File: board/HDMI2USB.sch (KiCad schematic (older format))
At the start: 0 parts

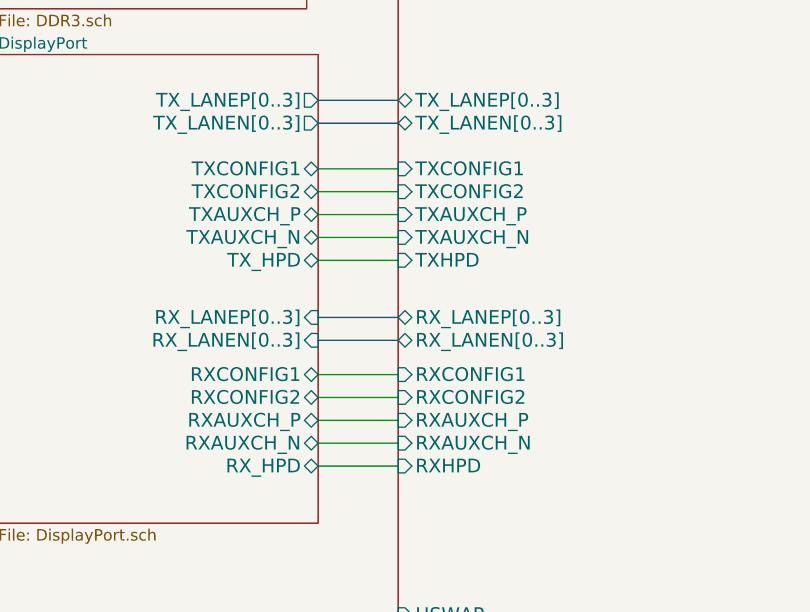
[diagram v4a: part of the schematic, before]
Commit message: Issue #1471 - usb Sheet changes
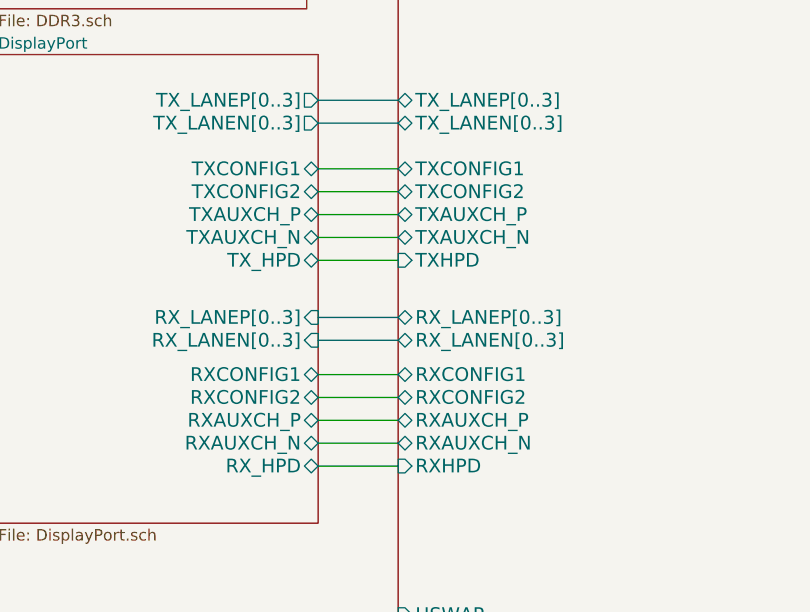
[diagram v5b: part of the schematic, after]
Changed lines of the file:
@@
 F22 "TX_LANEN[0..3]" B L 3750 4400 60
 F23 "TX_LANEP[0..3]" B L 3750 4300 60
-F24 "TXCONFIG1" I L 3750 4600 60
-F25 "TXCONFIG2" I L 3750 4700 60
-F26 "TXAUXCH_P" I L 3750 4800 60
-F27 "TXAUXCH_N" I L 3750 4900 60
+F24 "TXCONFIG1" B L 3750 4600 60
+F25 "TXCONFIG2" B L 3750 4700 60
+F26 "TXAUXCH_P" B L 3750 4800 60
+F27 "TXAUXCH_N" B L 3750 4900 60
 F28 "TXHPD" I L 3750 5000 60
-F29 "RXCONFIG1" I L 3750 5500 60
-F30 "RXCONFIG2" I L 3750 5600 60
-F31 "RXAUXCH_P" I L 3750 5700 60
+F29 "RXCONFIG1" B L 3750 5500 60
+F30 "RXCONFIG2" B L 3750 5600 60
+F31 "RXAUXCH_P" B L 3750 5700 60
 F32 "RXHPD" I L 3750 5900 60
-F33 "RXAUXCH_N" I L 3750 5800 60
+F33 "RXAUXCH_N" B L 3750 5800 60
 $EndSheet
 $Sheet

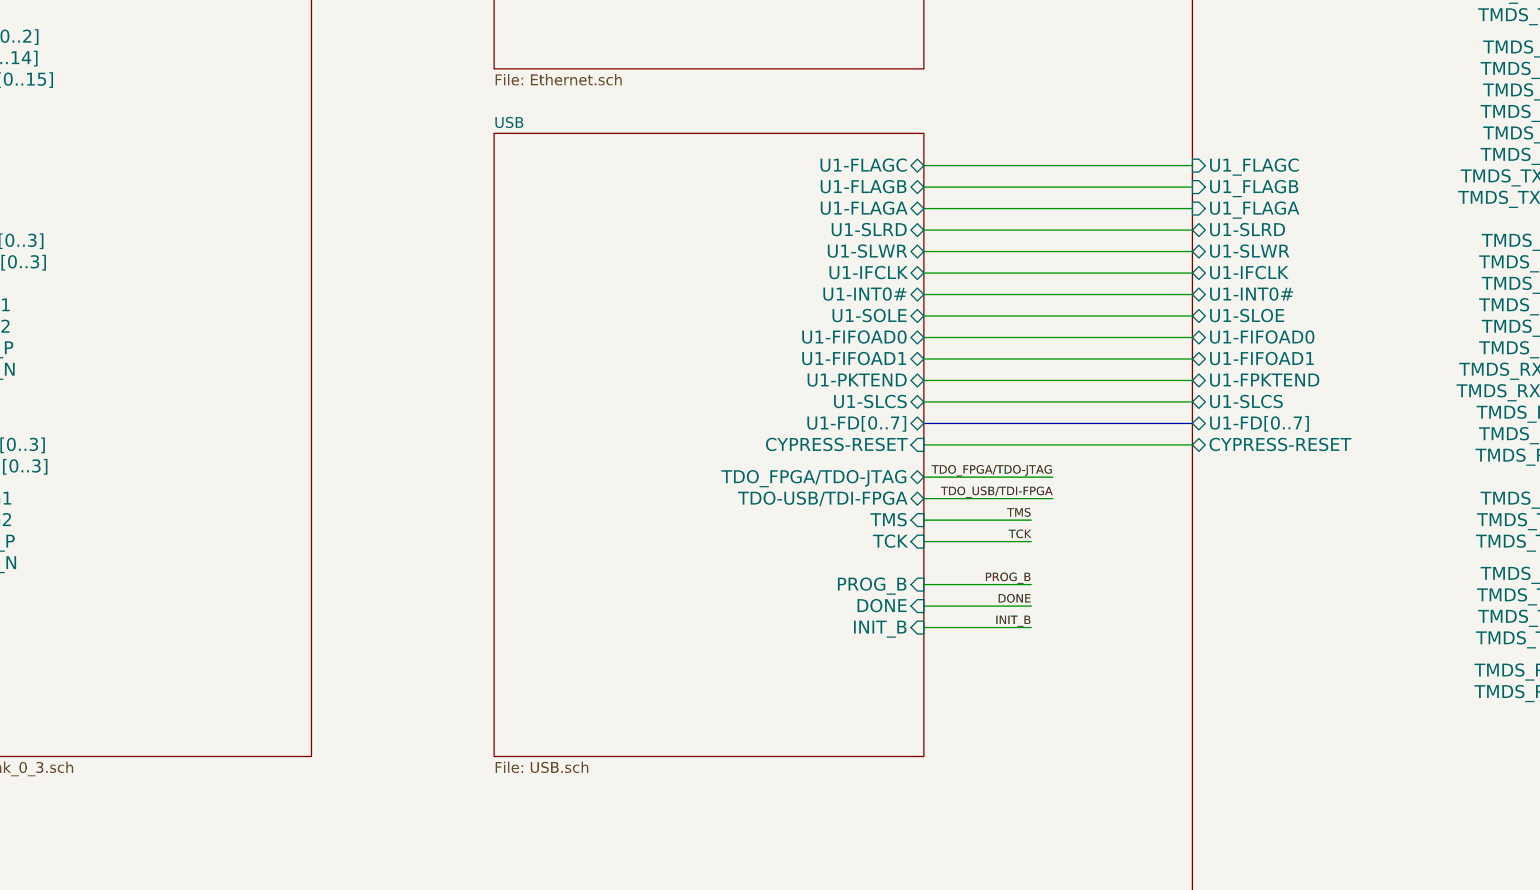
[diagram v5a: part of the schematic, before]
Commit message: Issue #1471 - USB schematic changes
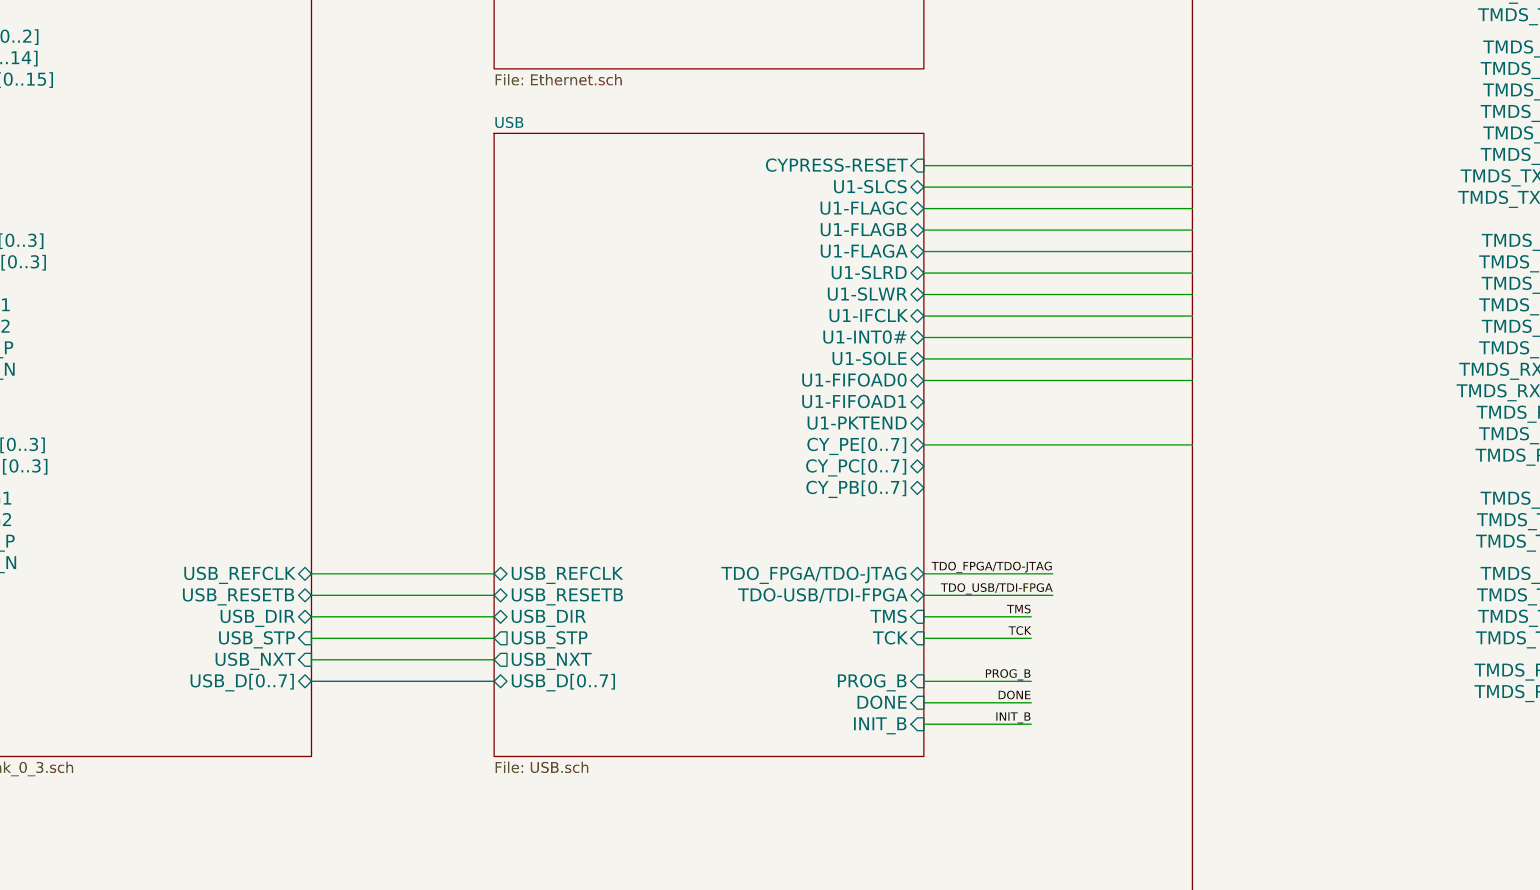
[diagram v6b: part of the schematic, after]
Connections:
- wire segments 125 -> 129

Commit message: Issue #1471 - Changes in Cypress
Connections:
- wire segments 129 -> 127
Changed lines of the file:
@@
 LIBS:valves
 LIBS:HDMI2USB-cache
+LIBS:1-cache
 EELAYER 27 0
 EELAYER END
@@
 Sheet 1 11
 Title "HDMI2USB"
-Date "1 jan 2015"
+Date "9 jan 2015"
 Rev "Rev2"
 Comp ""
@@
 F7 "DONE" I R 8550 6450 60
 F8 "INIT_B" I R 8550 6550 60
-F9 "CY_PE[0..7]" B R 8550 5250 60
-F10 "CY_PC[0..7]" B R 8550 5350 60
-F11 "CY_PB[0..7]" B R 8550 5450 60
-F12 "USB_D[0..7]" B L 6550 6350 60
-F13 "U1-FLAGC" B R 8550 4150 60
-F14 "U1-FLAGB" B R 8550 4250 60
-F15 "U1-FLAGA" B R 8550 4350 60
-F16 "U1-SLRD" B R 8550 4450 60
-F17 "U1-SLWR" B R 8550 4550 60
-F18 "U1-IFCLK" B R 8550 4650 60
-F19 "U1-INT0#" B R 8550 4750 60
-F20 "U1-SOLE" B R 8550 4850 60
-F21 "U1-FIFOAD0" B R 8550 4950 60
-F22 "U1-FIFOAD1" B R 8550 5050 60
-F23 "U1-PKTEND" B R 8550 5150 60
-F24 "U1-SLCS" B R 8550 4050 60
-F25 "CYPRESS-RESET" I R 8550 3950 60
-F26 "USB_NXT" O L 6550 6250 60
-F27 "USB_STP" O L 6550 6150 60
-F28 "USB_DIR" B L 6550 6050 60
-F29 "USB_RESETB" B L 6550 5950 60
-F30 "USB_REFCLK" B L 6550 5850 60
+F9 "USB_D[0..7]" B L 6550 6350 60
+F10 "CYPRESS-RESET" I R 8550 3950 60
+F11 "USB_NXT" O L 6550 6250 60
+F12 "USB_STP" O L 6550 6150 60
+F13 "USB_DIR" B L 6550 6050 60
+F14 "USB_RESETB" B L 6550 5950 60
+F15 "USB_REFCLK" B L 6550 5850 60
+F16 "U1-IFCLK" B R 8550 4050 60
+F17 "CY_PA[0..7]" B R 8550 4150 60
+F18 "CY_PC[0..7]" B R 8550 4250 60
+F19 "CY_FD[0..15]" B R 8550 4350 60
+F20 "CY_RD[0..5]" B R 8550 4450 60
+F21 "CY_CTL[0..5]" B R 8550 4550 60
+F22 "CY_WR" B R 8550 4650 60
+F23 "CY_RD" B R 8550 4750 60
+F24 "CY_T0" B R 8550 4850 60
+F25 "CY_RXD0" I R 8550 4950 60
+F26 "CY_RXD1" I R 8550 5050 60
+F27 "CY_TXD0" O R 8550 5150 60
+F28 "CY_TXD1" O R 8550 5250 60
+F29 "CY_INT5" O R 8550 5350 60
 $EndSheet
 Wire Wire Line
@@
 	8550 4050 9800 4050
 Wire Wire Line
-	9800 4150 8550 4150
-Wire Wire Line
+	8550 4650 9800 4650
+Wire Wire Line
+	9800 4750 8550 4750
+Wire Wire Line
+	8550 4850 9800 4850
+Wire Wire Line
+	8550 4950 9800 4950
+Wire Wire Line
+	8600 7800 9100 7800
+Wire Wire Line
+	8600 7900 9100 7900
+Wire Wire Line
+	8600 8100 9100 8100
+Wire Wire Line
+	8600 8200 9200 8200
+Wire Wire Line
+	8600 8400 9200 8400
+Wire Wire Line
+	8600 8600 9200 8600
+Wire Wire Line
+	8600 8000 9100 8000
+Wire Wire Line
+	9100 8300 8600 8300
+Wire Wire Line
+	8550 6350 9050 6350
+Wire Wire Line
+	8550 6550 9050 6550
+Wire Wire Line
+	8550 6150 9050 6150
+Wire Wire Line
+	8550 5950 9150 5950
+Wire Wire Line
+	8550 5850 9150 5850
+Wire Wire Line
+	8550 6450 9050 6450
+Wire Wire Line
+	9050 6050 8550 6050
+Wire Wire Line
+	8550 5250 9800 5250
+Wire Bus Line
+	8550 1500 9800 1500
+Wire Bus Line
+	9800 1600 8550 1600
+Wire Wire Line
+	8550 1700 9800 1700
+Wire Wire Line
+	9800 1800 8550 1800
+Wire Wire Line
+	8550 1900 9800 1900
+Wire Wire Line
+	8550 2000 9800 2000
+Wire Wire Line
+	8550 2100 9800 2100
+Wire Wire Line
+	8550 2200 9800 2200
+Wire Wire Line
+	8550 2300 9800 2300
+Wire Wire Line
+	8550 2400 9800 2400
+Wire Wire Line
+	8550 2500 9800 2500
+Wire Wire Line
+	8550 2600 9800 2600
+Wire Wire Line
+	8550 2700 9800 2700
+Wire Bus Line
+	3400 4300 3750 4300
+Wire Bus Line
+	3400 4400 3750 4400
+Wire Bus Line
+	3400 5350 3750 5350
+Wire Bus Line
+	3400 5250 3750 5250
+Wire Wire Line
+	3400 5500 3750 5500
+Wire Wire Line
+	3400 5600 3750 5600
+Wire Wire Line
+	3400 5700 3750 5700
+Wire Wire Line
+	3400 5800 3750 5800
+Wire Wire Line
+	3400 5900 3750 5900
+Wire Wire Line
+	3400 5000 3750 5000
+Wire Wire Line
+	3400 4900 3750 4900
+Wire Wire Line
+	3400 4800 3750 4800
+Wire Wire Line
+	3400 4700 3750 4700
+Wire Wire Line
+	3400 4600 3750 4600
+Wire Bus Line
+	6550 6350 5700 6350
+Wire Wire Line
+	6550 6250 5700 6250
+Wire Wire Line
+	6550 6150 5700 6150
+Wire Wire Line
+	6550 6050 5700 6050
+Wire Wire Line
+	6550 5950 5700 5950
+Wire Wire Line
+	6550 5850 5700 5850
+Wire Wire Line
+	8550 5150 9800 5150
+Wire Wire Line
+	8550 5050 9800 5050
+Wire Wire Line
+	8600 5350 9800 5350
+Wire Bus Line
+	8550 4550 9800 4550
+Wire Bus Line
+	8550 4450 9800 4450
+Wire Bus Line
+	8550 4350 9800 4350
+Wire Bus Line
 	8550 4250 9800 4250
-Wire Wire Line
-	9800 4350 8550 4350
-Wire Wire Line
-	8550 4450 9800 4450
-Wire Wire Line
-	9800 4550 8550 4550
-Wire Wire Line
-	8550 4650 9800 4650
-Wire Wire Line
-	9800 4750 8550 4750
-Wire Wire Line
-	8550 4850 9800 4850
-Wire Wire Line
-	8550 4950 9800 4950
-Wire Wire Line
-	8600 7800 9100 7800
-Wire Wire Line
-	8600 7900 9100 7900
-Wire Wire Line
-	8600 8100 9100 8100
-Wire Wire Line
-	8600 8200 9200 8200
-Wire Wire Line
-	8600 8400 9200 8400
-Wire Wire Line
-	8600 8600 9200 8600
-Wire Wire Line
-	8600 8000 9100 8000
-Wire Wire Line
-	9100 8300 8600 8300
-Wire Wire Line
-	8550 6350 9050 6350
-Wire Wire Line
-	8550 6550 9050 6550
-Wire Wire Line
-	8550 6150 9050 6150
-Wire Wire Line
-	8550 5950 9150 5950
-Wire Wire Line
-	8550 5850 9150 5850
-Wire Wire Line
-	8550 6450 9050 6450
-Wire Wire Line
-	9050 6050 8550 6050
-Wire Wire Line
-	8550 5250 9800 5250
-Wire Bus Line
-	8550 1500 9800 1500
-Wire Bus Line
-	9800 1600 8550 1600
-Wire Wire Line
-	8550 1700 9800 1700
-Wire Wire Line
-	9800 1800 8550 1800
-Wire Wire Line
-	8550 1900 9800 1900
-Wire Wire Line
-	8550 2000 9800 2000
-Wire Wire Line
-	8550 2100 9800 2100
-Wire Wire Line
-	8550 2200 9800 2200
-Wire Wire Line
-	8550 2300 9800 2300
-Wire Wire Line
-	8550 2400 9800 2400
-Wire Wire Line
-	8550 2500 9800 2500
-Wire Wire Line
-	8550 2600 9800 2600
-Wire Wire Line
-	8550 2700 9800 2700
-Wire Bus Line
-	3400 4300 3750 4300
-Wire Bus Line
-	3400 4400 3750 4400
-Wire Bus Line
-	3400 5350 3750 5350
-Wire Bus Line
-	3400 5250 3750 5250
-Wire Wire Line
-	3400 5500 3750 5500
-Wire Wire Line
-	3400 5600 3750 5600
-Wire Wire Line
-	3400 5700 3750 5700
-Wire Wire Line
-	3400 5800 3750 5800
-Wire Wire Line
-	3400 5900 3750 5900
-Wire Wire Line
-	3400 5000 3750 5000
-Wire Wire Line
-	3400 4900 3750 4900
-Wire Wire Line
-	3400 4800 3750 4800
-Wire Wire Line
-	3400 4700 3750 4700
-Wire Wire Line
-	3400 4600 3750 4600
-Wire Bus Line
-	6550 6350 5700 6350
-Wire Wire Line
-	6550 6250 5700 6250
-Wire Wire Line
-	6550 6150 5700 6150
-Wire Wire Line
-	6550 6050 5700 6050
-Wire Wire Line
-	6550 5950 5700 5950
-Wire Wire Line
-	6550 5850 5700 5850
+Wire Bus Line
+	8550 4150 9800 4150
 $EndSCHEMATC
